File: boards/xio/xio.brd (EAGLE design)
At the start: 170 x 170 mm, 241 parts, among them CN3 J00-0065NL, U2 LAN8742A-CZ, X2 USB-A, Y1 NX3225SA-12.000MHZ-STD-CSR-1, Y2 NX3225SA-12.000MHZ-STD-CSR-1, Y3 NX3225SA-25.000MHZ-STD-CSR-1

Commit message: Revision ready for routing for DR
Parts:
- added R10, R11, R5: 0R, rcl:R0402
- added R12, R13: 2.7k, rcl:R0402
- R2, R3, R4: value 330 -> 1K
- V33_0, V33_1, V33_2, V33_3, V33_4, V33_5, V33_6, VREG33: value AP7363-330-13 -> AP7363-33D-13
- moved R50 1.72 mm to (48.9, 27.9), turned to 180 degrees
- moved R49 1.68 mm to (48.3, 26.7), turned to 180 degrees
- moved C117 1.56 mm to (48.0, 19.0), turned to 90 degrees
- moved R48 1.55 mm to (46.0, 17.2), turned to 90 degrees
- moved R53 0.79 mm to (48.3, 21.6)
- moved R78 0.56 mm to (59.6, 23.6)
- moved R77 0.46 mm to (62.8, 23.6)
- moved C116 0.41 mm to (40.5, 15.3)
- moved R79 0.36 mm to (68.8, 23.6)
- moved VRE18 0.29 mm to (10.2, 38.7)
- moved VREG33 0.17 mm to (10.2, 50.2)
- moved C37 0.16 mm to (17.1, 142.2)
- moved C38 0.16 mm to (17.1, 143.5)
- moved V33_0 0.16 mm to (10.2, 142.9)
- moved R80 0.15 mm to (65.6, 23.6)
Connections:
- new net N$6: PIO.197, R10.1, R11.2
- net +3V3: now also R11.1, R5.1
- net +5V: now also R12.1, R13.1
- net DDSCL: now also R12.2
- net DDSDA: now also R13.2
- net GND: now also R10.2, SLOT0.B9, SLOT1.B15, SLOT2.B13, SLOT2.B9, SLOT3.B13, SLOT3.B15, SLOT4.B9, SLOT6.B11, SLOT6.B13, SLOT6.B9; no longer PIO.197, SLOT2.B12, SLOT3.B12, SLOT4.B15, SLOT6.B12, SLOT6.B15
- net N$11: now also R5.2
- net S1_V33: no longer SLOT0.B9
- net S2_V33: no longer SLOT1.B15
- net S3_V33: now also SLOT2.B12; no longer SLOT2.B13, SLOT2.B9
- net S4_V33: now also SLOT3.B12; no longer SLOT3.B13
- net S5_V33: now also SLOT4.B15; no longer SLOT4.B9
- net S7_V33: now also SLOT6.B12, SLOT6.B15; no longer SLOT6.B11, SLOT6.B13, SLOT6.B9
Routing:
- net +3V3: track 1015.9 -> 0.00 mm, vias 34 -> 0
- net GND: track 918.4 -> 0.00 mm, vias 62 -> 0
- net +5V: track 369.2 -> 0.00 mm, vias 11 -> 72
- net VHDCI_AUDIO_SIO: track 368.0 -> 0.00 mm, vias 4 -> 0
- net VHDCI_AUDIO_L: track 358.2 -> 0.00 mm, vias 4 -> 0
- net VHDCI_A5: track 348.3 -> 0.00 mm, vias 6 -> 0
- net VHDCI_A8: track 346.2 -> 0.00 mm, vias 3 -> 0
- net VHDCI_A12: track 339.8 -> 0.00 mm, vias 3 -> 0
- net VHDCI_AUDIO_R: track 337.2 -> 0.00 mm, vias 3 -> 0
- net VHDCI_A6: track 336.2 -> 0.00 mm, vias 7 -> 0
- net VHDCI_A2: track 334.2 -> 0.00 mm, vias 4 -> 0
- net I2C_SCL: track 328.1 -> 0.00 mm, vias 3 -> 0
- net VHDCI_D2: track 325.5 -> 0.00 mm, vias 6 -> 0
- net I2C_SDA: track 324.2 -> 0.00 mm, vias 4 -> 0
- net VHDCI_A1: track 320.9 -> 0.00 mm, vias 4 -> 0
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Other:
- board text added: "1mm max len diff"
- board text added: "TX:4mm RX: 6mm"
- board text removed: "Add vias to +3v3 around vRegs XIO:BOOT0 ought to have no-stuff pull-up Label for XIO:XSPI XIO:LED ought to be 1k ? XIO:PSRAM - check pins XIO:Serial IO - move gnd/power pins PIO:BOOT0 needs pullup/down Labels for SD-Card and ADC sections Notes on SDRAM lengths Label for Audio/video section into HDMI Move PIO:Video-in to 14/19"

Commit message: Checkpoint
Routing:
- net +3V3: track 0.00 -> 933.1 mm, vias 0 -> 22
- net VHDCI_A11: track 0.00 -> 383.4 mm, vias 0 -> 15
- net VHDCI_A0: track 0.00 -> 368.1 mm, vias 0 -> 10
- net VHDCI_AUDIO_SIO: track 0.00 -> 360.9 mm, vias 0 -> 17
- net !VHDCI_MPD!: track 0.00 -> 356.5 mm, vias 0 -> 12
- net VHDCI_AUDIO_R: track 0.00 -> 349.3 mm, vias 0 -> 24
- net VHDCI_AUDIO_L: track 0.00 -> 344.3 mm, vias 0 -> 23
- net VHDCI_A9: track 0.00 -> 332.5 mm, vias 0 -> 17
- net VHDCI_D1: track 0.00 -> 332.4 mm, vias 0 -> 21
- net VHDCI_A6: track 0.00 -> 330.8 mm, vias 0 -> 14
- net VHDCI_A8: track 0.00 -> 329.5 mm, vias 0 -> 11
- net VHDCI_REF: track 0.00 -> 328.4 mm, vias 0 -> 16
- net VHDCI_RST: track 0.00 -> 325.5 mm, vias 0 -> 12
- net VHDCI_A12: track 0.00 -> 324.4 mm, vias 0 -> 10
- net VHDCI_A10: track 0.00 -> 323.2 mm, vias 0 -> 14
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
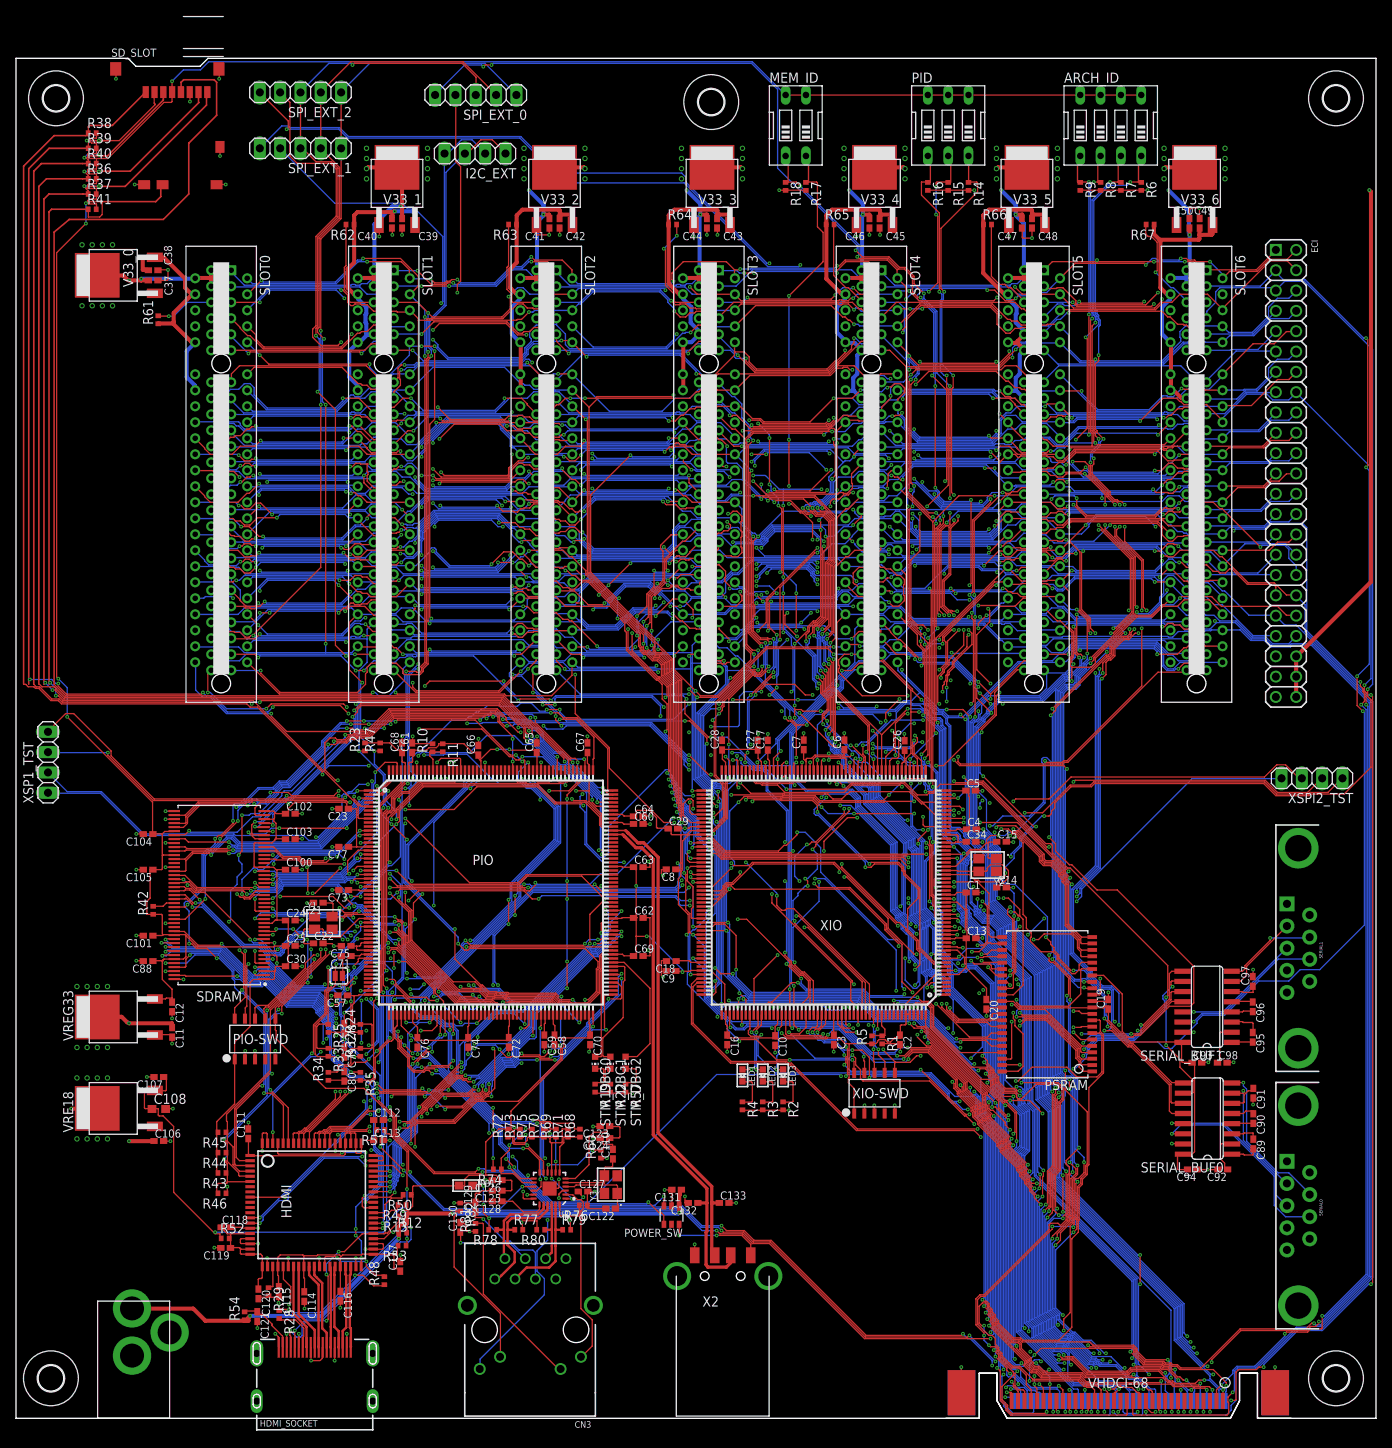
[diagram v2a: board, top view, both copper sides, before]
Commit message: Latest routed board, change out the solder bridge for a 0-ohm resistor
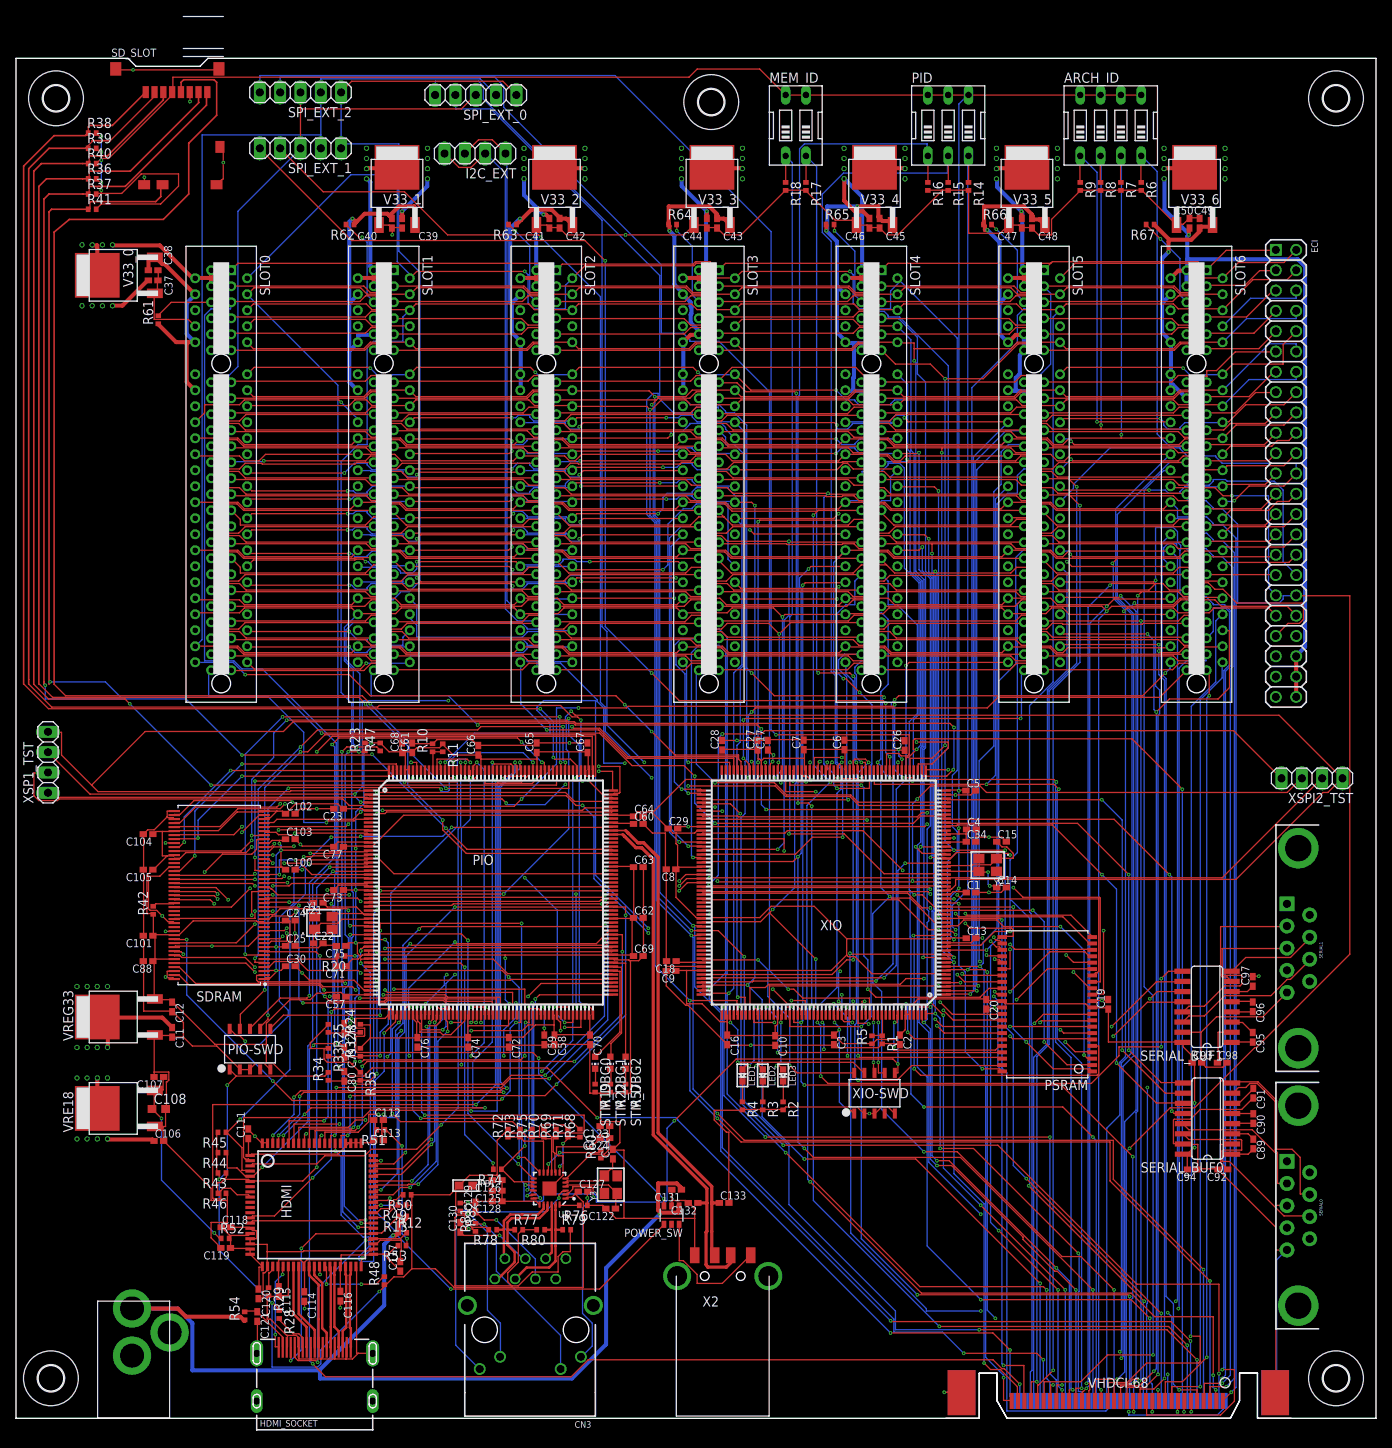
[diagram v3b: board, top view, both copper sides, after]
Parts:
- removed SJ1: SOLDERJUMPERNC, SparkFun:SJ_2S
- added R20: 0R, rcl:R0402
- moved PIO-SWD 1.42 mm to (29.3, 46.1)
- moved C71 1.42 mm to (40.6, 56.5)
- moved C23 0.64 mm to (40.3, 76.2)
- moved C73 0.64 mm to (40.3, 66.0)
- moved C77 0.64 mm to (40.3, 71.4)
- moved C75 0.63 mm to (40.6, 59.1)
- moved C57 0.26 mm to (40.6, 52.7)
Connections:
- net N$100 renamed STM_RAM_DQM2
- net N$101 renamed STM_RAM_DQM3
- net N$102 renamed STM_RAM_RAS
- net N$103 renamed STM_RAM_CAS
- net N$104 renamed STM_RAM_WE
- net N$97 renamed STM_RAM_CLK
- net N$98 renamed STM_RAM_DQM0
- net N$99 renamed STM_RAM_DQM1
- net AGND: now also R20.1; no longer SJ1.2
- net GND: now also R20.2; no longer SJ1.1
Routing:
- net GND: track 294.9 -> 870.8 mm, vias 180 -> 60
- net +3V3: track 933.1 -> 1114.2 mm, vias 22 -> 30
- net +5V: track 308.2 -> 398.4 mm, vias 93 -> 79
- net VHDCI_A11: track 383.4 -> 309.8 mm, vias 15 -> 7
- net VHDCI_A0: track 368.1 -> 295.2 mm, vias 10 -> 3
- net SPI_IRQ5: track 147.1 -> 76.0 mm, vias 1 -> 2
- net N$109: track 118.1 -> 49.1 mm
- net !VHDCI_MPD!: track 356.5 -> 288.6 mm, vias 12 -> 4
- net VHDCI_D7: track 308.3 -> 258.0 mm, vias 15 -> 4
- net N$114: track 103.1 -> 54.1 mm, vias 3 -> 2
- net VHDCI_J1_A2: track 279.6 -> 231.0 mm, vias 11 -> 3
- net VHDCI_D1: track 332.4 -> 284.3 mm, vias 21 -> 3
- net VHDCI_J1_A1: track 292.4 -> 244.7 mm, vias 14 -> 7
- net VHDCI_A14: track 307.1 -> 262.0 mm, vias 21 -> 3
- net VHDCI_J1_5: track 280.8 -> 237.7 mm, vias 9 -> 4
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
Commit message: Move some caps to be closer to their pins Add some more information text to the schematics
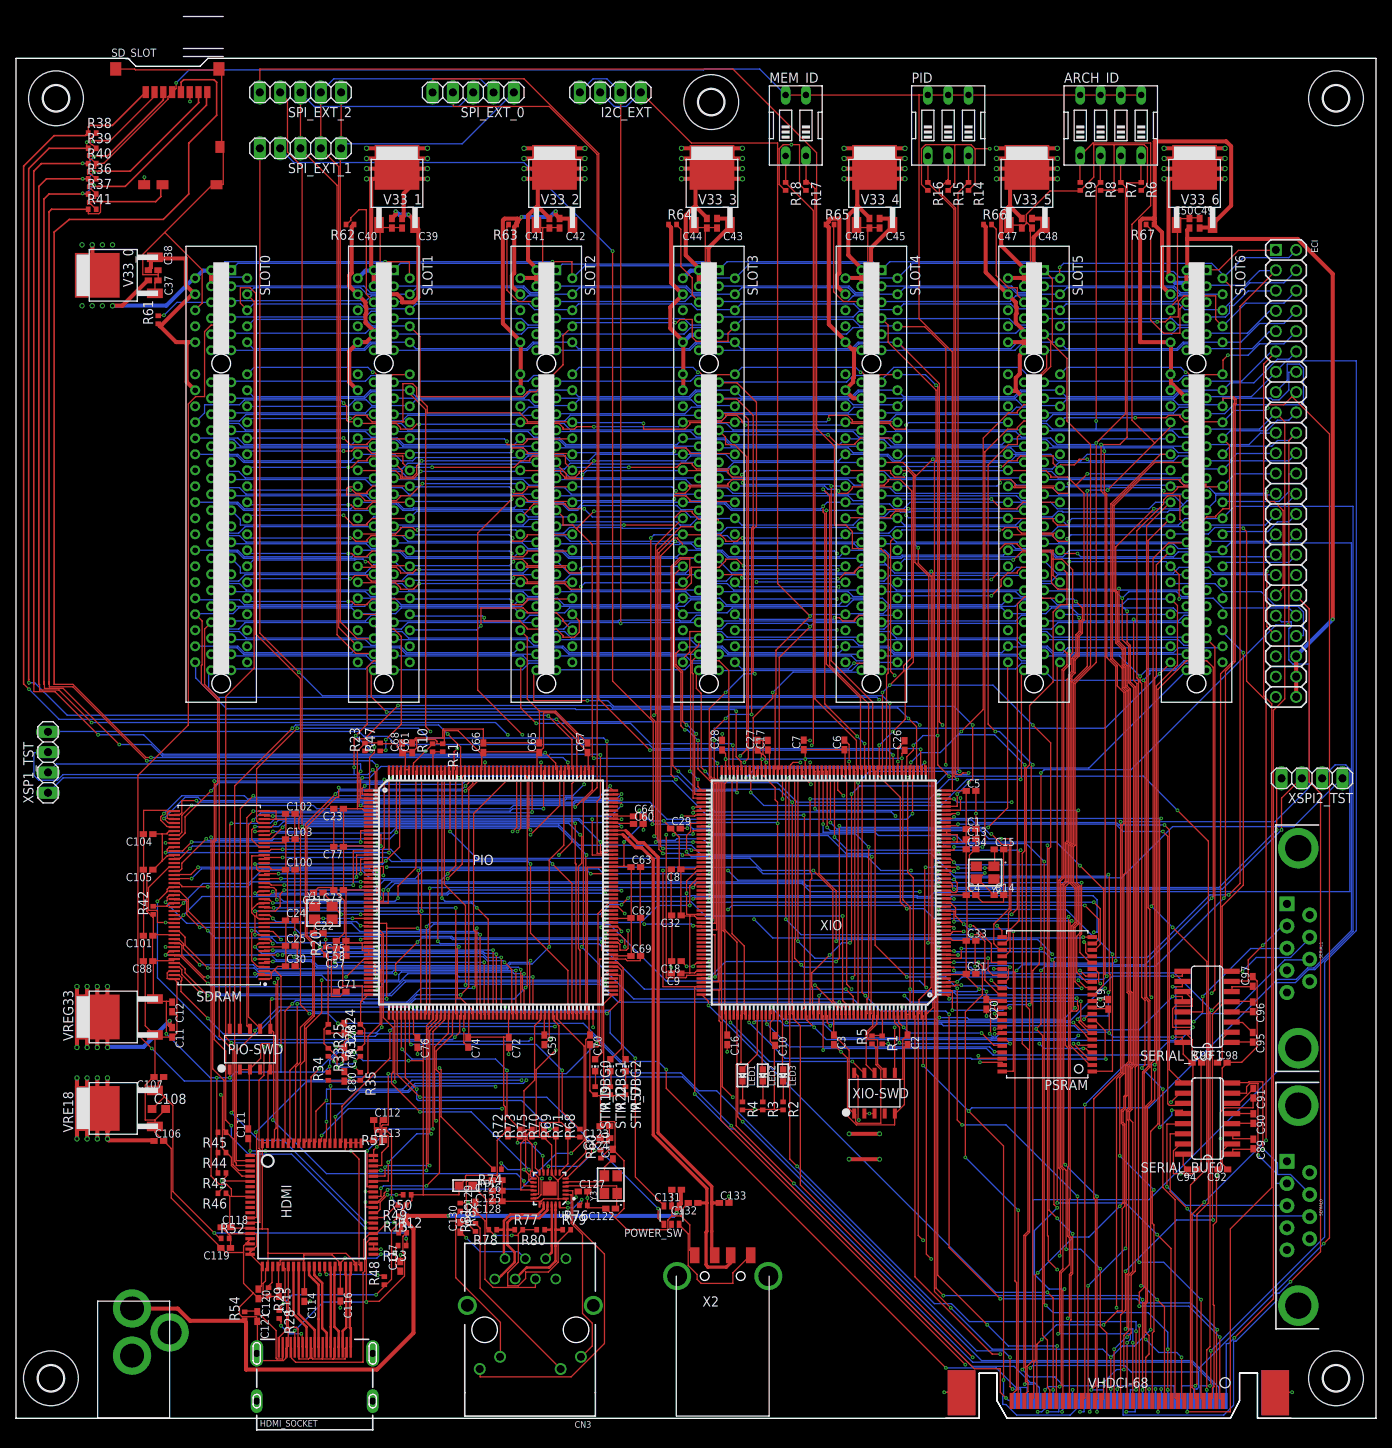
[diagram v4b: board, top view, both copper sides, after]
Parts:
- added C31, C32, C33: 0.1uF, rcl:C0402K
- moved C58 29.0 mm to (40.6, 58.7), turned to 180 degrees
- moved I2C_EXT 18.6 mm to (74.3, 165.7)
- moved C13 12.4 mm to (119.4, 72.4)
- moved C4 8.22 mm to (119.4, 65.4)
- moved C1 7.94 mm to (119.4, 73.7)
- moved C57 5.08 mm to (40.6, 57.8)
- moved C71 3.17 mm to (40.6, 53.3), turned to 0 degrees
- moved R20 2.01 mm to (38.7, 58.4), turned to 90 degrees
- moved C21 1.27 mm to (37.8, 65.7)
- moved C22 1.27 mm to (37.8, 60.6)
- moved Y1 1.27 mm to (38.4, 63.2)
- moved C14 1.00 mm to (122.9, 65.4)
- moved C15 1.00 mm to (122.9, 71.1)
- moved Y2 1.00 mm to (121.1, 68.2)
- moved C2 0.95 mm to (111.4, 47.3)
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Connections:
- net +3V3: now also C31.1, C32.1, C33.1
- net GND: now also C31.2, C32.2, C33.2
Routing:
- net +5V: track 398.4 -> 506.5 mm, vias 79 -> 76
- net XSPI2_SSEL: track 199.3 -> 133.4 mm, vias 2 -> 3
- net +3V3: track 1114.2 -> 1051.5 mm, vias 30 -> 32
- net VHDCI_D6: track 254.7 -> 314.3 mm
- net VHDCI_D2: track 284.5 -> 343.7 mm, vias 7 -> 4
- net VHDCI_D1XX: track 271.7 -> 328.9 mm, vias 7 -> 10
- net VHDCI_A11: track 309.8 -> 365.4 mm
- net I2C_SCL: track 298.1 -> 347.5 mm
- net VHDCI_A8: track 311.9 -> 361.1 mm, vias 5 -> 4
- net XSPI1_CLK: track 166.6 -> 120.3 mm
- net VHDCI_A12: track 298.4 -> 340.8 mm, vias 2 -> 3
- net S7_V33: track 32.9 -> 72.2 mm, vias 1 -> 0
- net LCD_G5: track 92.8 -> 54.0 mm, vias 2 -> 3
- net XSPI2_CLK: track 165.1 -> 126.6 mm
- net GND: track 870.8 -> 904.9 mm, vias 60 -> 69
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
